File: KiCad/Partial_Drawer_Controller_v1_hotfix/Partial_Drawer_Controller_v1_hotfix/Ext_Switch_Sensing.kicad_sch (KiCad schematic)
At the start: 4 parts

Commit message: chore: updates parts and BOM export for `Partial_Drawer_Controller_v1_hotfix`
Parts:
- C67: path_to_docs (none) -> Passive_Components/Capacitors/MLCC/Samsung_Electro-Mechanics
- R208, R209: path_to_docs (none) -> Passive_Components/Resistors/UNI-ROYAL
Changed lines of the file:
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@@
+			)
+		)
+		(property "OC_CONRAD" ""
+			(at 139.7 85.09 0)
+			(effects
+				(font
+					(size 1.27 1.27)
+				)
+				(hide yes)
+			)
+		)
+		(property "OC_RS" ""
+			(at 139.7 85.09 0)
+			(effects
+				(font
+					(size 1.27 1.27)
+				)
+				(hide yes)
+			)
+		)
+		(property "path_to_docs" "Passive_Components/Resistors/UNI-ROYAL"
+			(at 139.7 85.09 0)
+			(effects
+				(font
+					(size 1.27 1.27)
+				)
+				(hide yes)
 			)
 		)
@@
 			)
 		)
-		(property "Description" ""
+		(property "Description" "Power symbol creates a global label with name \"GND\" , ground"
 			(at 128.27 96.52 0)
 			(effects
@@
 			)
 		)
+		(property "OC_CONRAD" ""
+			(at 151.13 78.74 0)
+			(effects
+				(font
+					(size 1.27 1.27)
+				)
+				(hide yes)
+			)
+		)
+		(property "OC_RS" ""
+			(at 151.13 78.74 0)
+			(effects
+				(font
+					(size 1.27 1.27)
+				)
+				(hide yes)
+			)
+		)
+		(property "path_to_docs" "Passive_Components/Resistors/UNI-ROYAL"
+			(at 151.13 78.74 0)
+			(effects
+				(font
+					(size 1.27 1.27)
+				)
+				(hide yes)
+			)
+		)
 		(pin "1"
 		)
@@
 			)
 		)
-		(property "Description" ""
+		(property "Description" "Power symbol creates a global label with name \"GND\" , ground"
 			(at 157.48 96.52 0)
 			(effects
@@
 			)
 		)
+		(property "OC_CONRAD" ""
+			(at 128.27 91.44 0)
+			(effects
+				(font
+					(size 1.27 1.27)
+				)
+				(hide yes)
+			)
+		)
+		(property "OC_RS" ""
+			(at 128.27 91.44 0)
+			(effects
+				(font
+					(size 1.27 1.27)
+				)
+				(hide yes)
+			)
+		)
+		(property "path_to_docs" "Passive_Components/Capacitors/MLCC/Samsung_Electro-Mechanics"
+			(at 128.27 91.44 0)
+			(effects
+				(font
+					(size 1.27 1.27)
+				)
+				(hide yes)
+			)
+		)
 		(pin "1"
 		)
@@
 			)
 		)
-		(property "Description" ""
+		(property "Description" "Power symbol creates a global label with name \"+3.3V\""
 			(at 151.13 73.66 0)
 			(effects

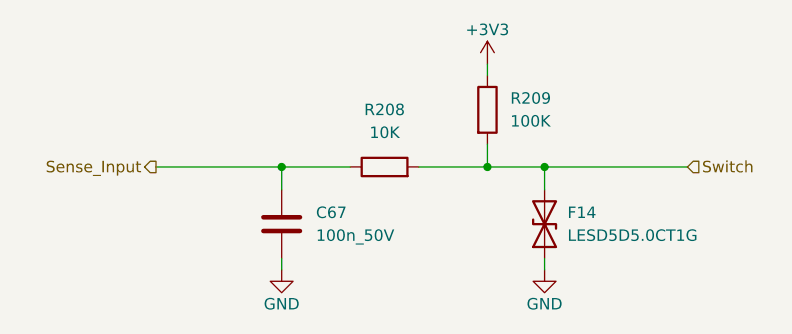
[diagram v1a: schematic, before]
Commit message: chore: updates symbols for `Partial_Drawer_Controller_v1_hotfix` to get docs for every part (not finished yet)
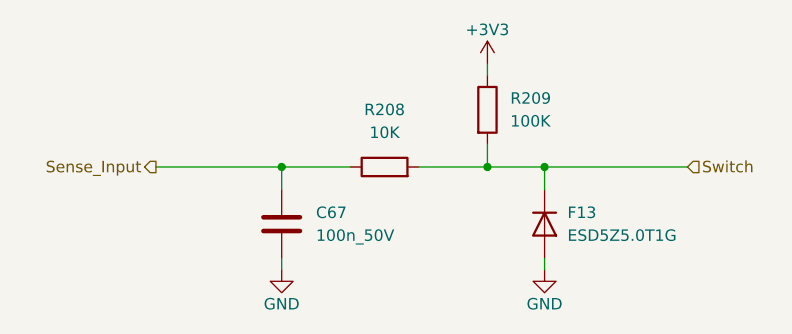
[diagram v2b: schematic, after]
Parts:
- removed F14: LESD5D5.0CT1G, Diode_SMD:D_SOD-523, symbol _Diode_TVS:LESD5D5.0CT1G
- added F13: ESD5Z5.0T1G, Diode_SMD:D_SOD-523, symbol _Diode_TVS:ESD5Z5.0T1G
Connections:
- net GND: now also F13.2 (A)
- net Switch: now also F13.1 (K)
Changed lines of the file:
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@@
+	)
+	(symbol
+		(lib_id "_Diode_TVS:ESD5Z5.0T1G")
+		(at 157.48 91.44 270)
+		(unit 1)
+		(exclude_from_sim no)
+		(in_bom yes)
+		(on_board yes)
+		(dnp no)
+		(fields_autoplaced yes)
+		(property "Reference" "F13"
+			(at 160.02 90.1699 90)
+			(effects
+				(font
+					(size 1.27 1.27)
+				)
+				(justify left)
+			)
+		)
+		(property "Value" "ESD5Z5.0T1G"
+			(at 160.02 92.7099 90)
+			(effects
+				(font
+					(size 1.27 1.27)
+				)
+				(justify left)
+			)
+		)
+		(property "Footprint" "Diode_SMD:D_SOD-523"
+			(at 157.48 91.44 0)
+			(effects
+				(font
+					(size 1.27 1.27)
+				)
+				(hide yes)
+			)
+		)
+		(property "Datasheet" "https://www.mouser.de/datasheet/2/308/1/ESD5Z2_5T1_D-2311718.pdf"
+			(at 157.48 91.44 0)
+			(effects
+				(font
+					(size 1.27 1.27)
+				)
+				(hide yes)
+			)
+		)
+		(property "Description" "5V 174W TVS Diode Unidirectional"
+			(at 157.48 91.44 0)
+			(effects
+				(font
+					(size 1.27 1.27)
+				)
+				(hide yes)
+			)
+		)
+		(property "Sim.Device" "D"
+			(at 157.48 91.44 0)
+			(effects
+				(font
+					(size 1.27 1.27)
+				)
+				(hide yes)
+			)
+		)
+		(property "Sim.Pins" "1=K 2=A"
+			(at 157.48 91.44 0)
+			(effects
+				(font
+					(size 1.27 1.27)
+				)
+				(hide yes)
+			)
+		)
+		(property "MF" "onsemi"
+			(at 157.48 91.44 0)
+			(effects
+				(font
+					(size 1.27 1.27)
+				)
+				(hide yes)
+			)
+		)
+		(property "MPN" "ESD5Z5.0T1G"
+			(at 157.48 91.44 0)
+			(effects
+				(font
+					(size 1.27 1.27)
+				)
+				(hide yes)
+			)
+		)
+		(property "OC_CONRAD" ""
+			(at 157.48 91.44 0)
+			(effects
+				(font
+					(size 1.27 1.27)
+				)
+				(hide yes)
+			)
+		)
+		(property "OC_LCSC" "C82044"
+			(at 157.48 91.44 0)
+			(effects
+				(font
+					(size 1.27 1.27)
+				)
+				(hide yes)
+			)
+		)
+		(property "OC_MOUSER" "863-ESD5Z5.0T5G"
+			(at 157.48 91.44 0)
+			(effects
+				(font
+					(size 1.27 1.27)
+				)
+				(hide yes)
+			)
+		)
+		(property "OC_RS" ""
+			(at 157.48 91.44 0)
+			(effects
+				(font
+					(size 1.27 1.27)
+				)
+				(hide yes)
+			)
+		)
+		(property "path_to_docs" "Circuit_Protection/ESD_Protection_Diodes_TVS_Diodes/onsemi"
+			(at 157.48 91.44 0)
+			(effects
+				(font
+					(size 1.27 1.27)
+				)
+				(hide yes)
+			)
+		)
+		(pin "2"
+		)
+		(pin "1"
+		)
+		(instances
+			(project ""
+				(path "/57f8c193-fe09-43d3-9441-dbd40881d2aa/289ed4a0-c0fb-403f-8449-e46a308dbcad"
+					(reference "F13")
+					(unit 1)
+				)
+			)
+		)
 	)
 	(symbol
@@
 					(unit 1)
 				)
-			)
-		)
-	)
-	(symbol
-		(lib_id "_Diode_TVS:LESD5D5.0CT1G")
-		(at 157.48 91.44 90)
-		(unit 1)
-		(exclude_from_sim no)
-		(in_bom yes)
-		(on_board yes)
-		(dnp no)
-		(fields_autoplaced yes)
-		(property "Reference" "F14"
-			(at 160.02 90.1699 90)
-			(effects
-				(font
-					(size 1.27 1.27)
-				)
-				(justify right)
-			)
-		)
-		(property "Value" "LESD5D5.0CT1G"
-			(at 160.02 92.7099 90)
-			(effects
-				(font
-					(size 1.27 1.27)
-				)
-				(justify right)
-			)
-		)
-		(property "Footprint" "Diode_SMD:D_SOD-523"
-			(at 157.48 91.44 0)
-			(effects
-				(font
-					(size 1.27 1.27)
-				)
-				(hide yes)
-			)
-		)
-		(property "Datasheet" "https://datasheet.lcsc.com/lcsc/1912111437_LRC-LESD5D5-0CT1G_C383211.pdf"
-			(at 157.48 91.44 0)
-			(effects
-				(font
-					(size 1.27 1.27)
-				)
-				(hide yes)
-			)
-		)
-		(property "Description" "5V 150W TVS Diode Bi-Directional"
-			(at 157.48 91.44 0)
-			(effects
-				(font
-					(size 1.27 1.27)
-				)
-				(hide yes)
-			)
-		)
-		(property "MF" "LRC"
-			(at 157.48 91.44 0)
-			(effects
-				(font
-					(size 1.27 1.27)
-				)
-				(hide yes)
-			)
-		)
-		(property "MPN" "LESD5D5.0CT1G"
-			(at 157.48 91.44 0)
-			(effects
-				(font
-					(size 1.27 1.27)
-				)
-				(hide yes)
-			)
-		)
-		(property "OC_LCSC" "C383211"
-			(at 157.48 91.44 0)
-			(effects
-				(font
-					(size 1.27 1.27)
-				)
-				(hide yes)
-			)
-		)
-		(property "OC_MOUSER" ""
-			(at 157.48 91.44 0)
-			(effects
-				(font
-					(size 1.27 1.27)
-				)
-				(hide yes)
-			)
-		)
-		(pin "1"
-		)
-		(pin "2"
-		)
-		(instances
-			(project "Partial_Drawer_Controller_v1"
-				(path "/57f8c193-fe09-43d3-9441-dbd40881d2aa/289ed4a0-c0fb-403f-8449-e46a308dbcad"
-					(reference "F14")
-					(unit 1)
-				)
